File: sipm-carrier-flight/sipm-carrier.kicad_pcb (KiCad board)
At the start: 2 copper layers, 95 x 50 mm, 70 parts, among them J1 Conn_Coaxial_Small, J2 output, J3 Conn_02x02_Top_Bottom, U1 LTC6268xS8-10, U13 ADP7185ACPZN2.5-R7, U14 TPS7A2025PDBVR, U2 BUF602xD

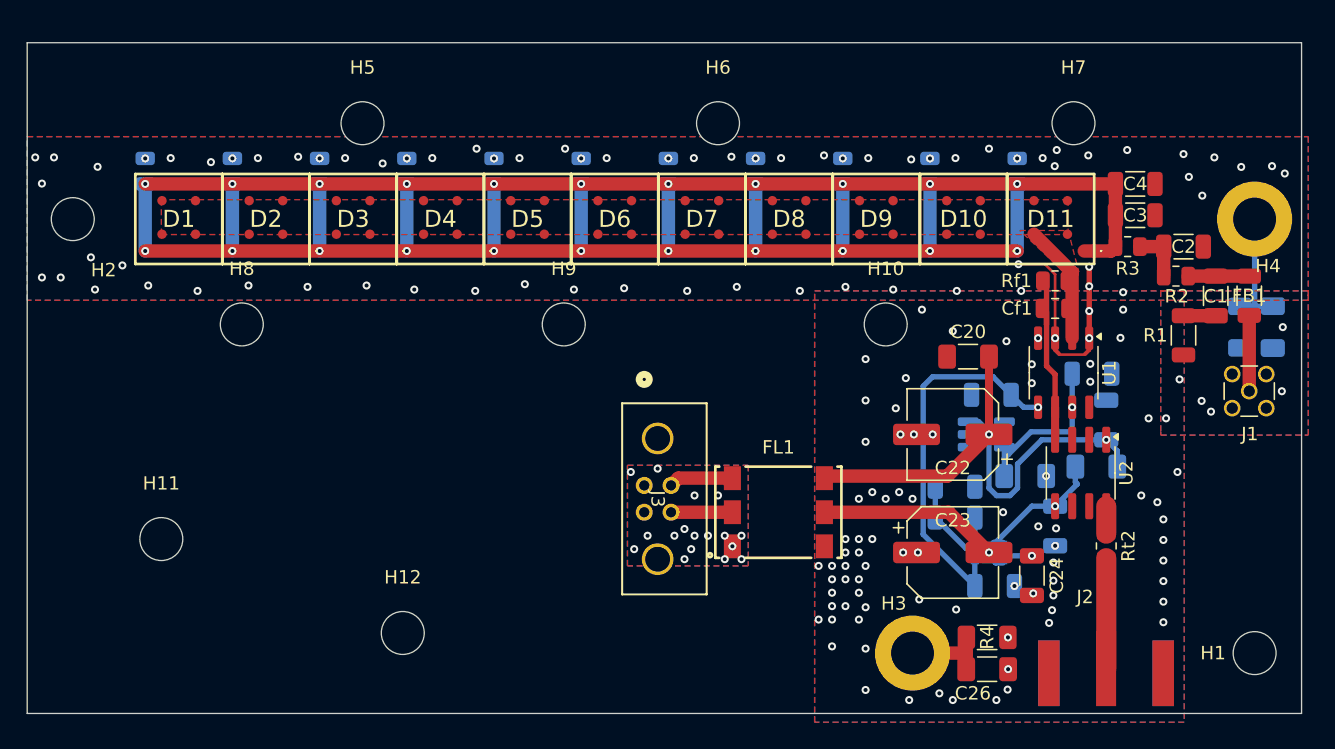
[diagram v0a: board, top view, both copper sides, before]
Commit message: updated per MSU comments
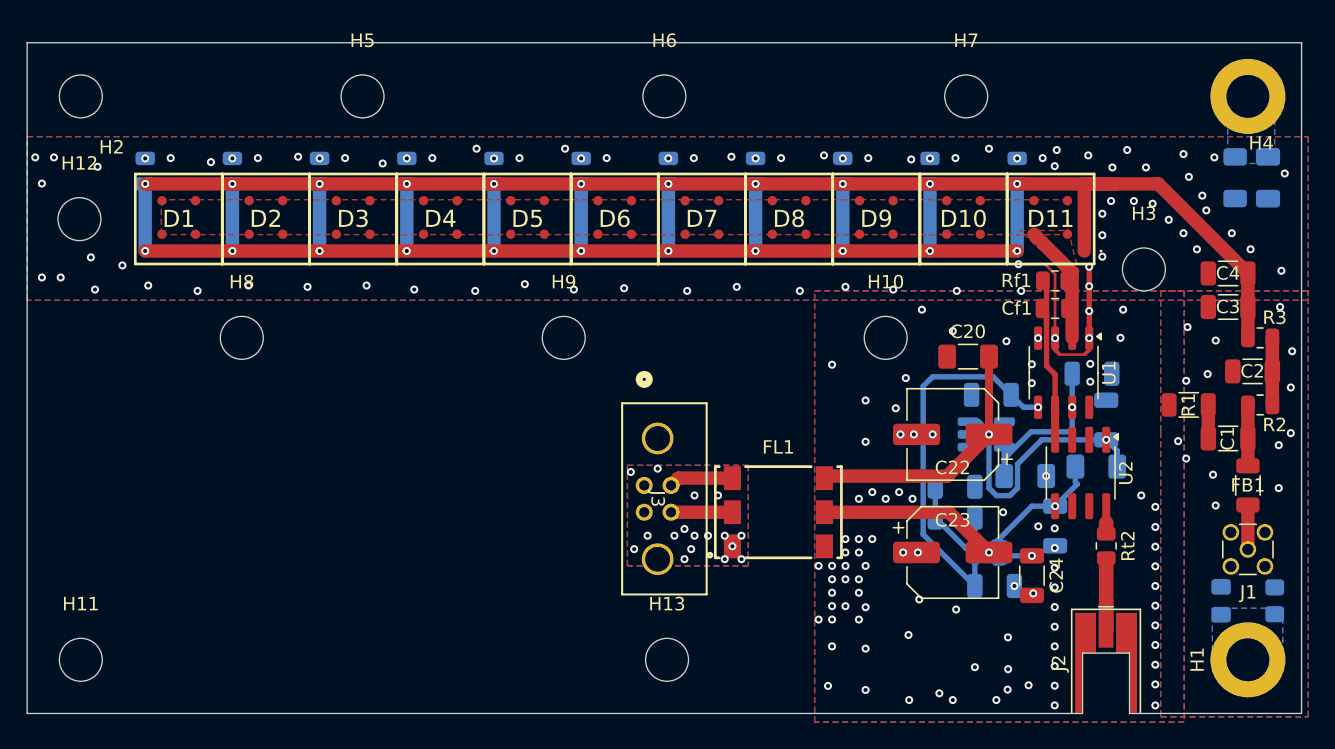
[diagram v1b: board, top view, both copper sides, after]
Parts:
- added H13: MountingHole, MountingHole:MountingHole_3.2mm_M3, F.Cu at (76.7, 72.0)
- C26: footprint Capacitor_SMD:C_1206_3216Metric_Pad1.33x1.80mm_HandSolder -> Capacitor_SMD:C_0805_2012Metric_Pad1.18x1.45mm_HandSolder; moved to B.Cu
- H1: value MountingHole -> MountingHole_Pad; footprint MountingHole:MountingHole_3.2mm_M3 -> MountingHole:MountingHole_3.2mm_M3_DIN965_Pad
- H3: value MountingHole_Pad -> MountingHole; footprint MountingHole:MountingHole_3.2mm_M3_DIN965_Pad -> MountingHole:MountingHole_3.2mm_M3
- J2: footprint Library:TE_CONSMA020.062-G -> Connector_Coaxial:MMCX_Molex_73415-0961_Horizontal_1.6mm-PCB
- R4: value 1.5Meg -> R_US; footprint Resistor_SMD:R_1206_3216Metric_Pad1.30x1.75mm_HandSolder -> Resistor_SMD:R_0805_2012Metric_Pad1.20x1.40mm_HandSolder; moved to B.Cu
- moved H12 39.1 mm to (32.9, 39.1)
- moved H3 33.4 mm to (112.2, 42.9)
- moved R4 21.6 mm to (122.0, 67.6), turned to -90 degrees
- moved C26 18.2 mm to (118.0, 67.6), turned to 90 degrees
- moved FB1 14.1 mm to (120.0, 59.0)
- moved R3 12.0 mm to (120.9, 48.0)
- moved J1 11.8 mm to (120.0, 63.8)
- moved R2 11.5 mm to (120.9, 53.0), turned to 180 degrees
- moved C27 11.1 mm to (121.5, 36.1)
- moved R5 11.1 mm to (119.0, 36.1)
- moved H11 10.8 mm to (33.0, 72.0)
- moved C1 10.7 mm to (118.5, 55.5), turned to 180 degrees
- moved C2 10.6 mm to (120.3, 50.5), turned to 180 degrees
- moved C3 9.73 mm to (118.5, 45.7), turned to 180 degrees
- moved C4 9.62 mm to (118.5, 43.2), turned to 180 degrees
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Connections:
- C26 pad 1: GND -> Net-(C26-Pad1)
- C26 pad 2: Net-(C26-Pad2) -> GND
- R4 pad 2: Net-(C26-Pad2) -> Net-(C26-Pad1)
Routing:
- net /Bias filter/bias_filtered: track 199.5 -> 217.1 mm
- net Net-(C27-Pad2): track 9.01 -> 0.00 mm
- net Net-(C26-Pad2): track 6.17 -> 0.00 mm
- net /driven TIA/amp_out: track 8.23 -> 5.30 mm
- net /Bias filter/bias_raw: track 5.64 -> 3.31 mm
- net Net-(Rt2-Pad1): track 2.05 -> 0.40 mm
- net Net-(C2-Pad1): track 3.97 -> 5.00 mm
- net -5V: track 26.9 -> 25.9 mm
- net Net-(FL1-1): track 5.56 -> 4.79 mm
- net GND: vias 160 -> 189
- added copper zone on B.Cu, net Net-(C26-Pad1)
- added copper zone on B.Cu, net Net-(C27-Pad2)
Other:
- outline, holes or cut-outs redrawn

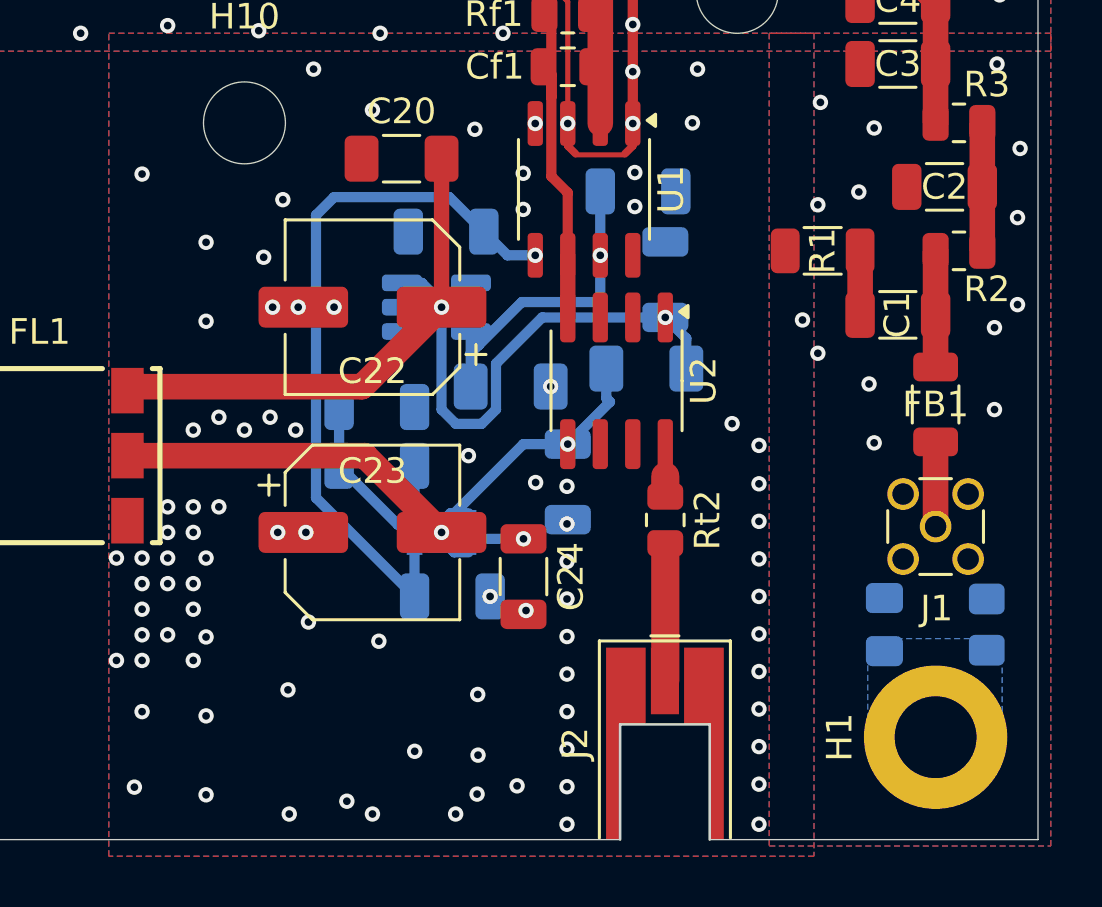
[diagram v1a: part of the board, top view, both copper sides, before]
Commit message: carrier OCD
- coplanar waveguide with ground at almost exactly 50 ohm output from the buffer, leading into termination resistor
- better ground return paths for the bias voltage
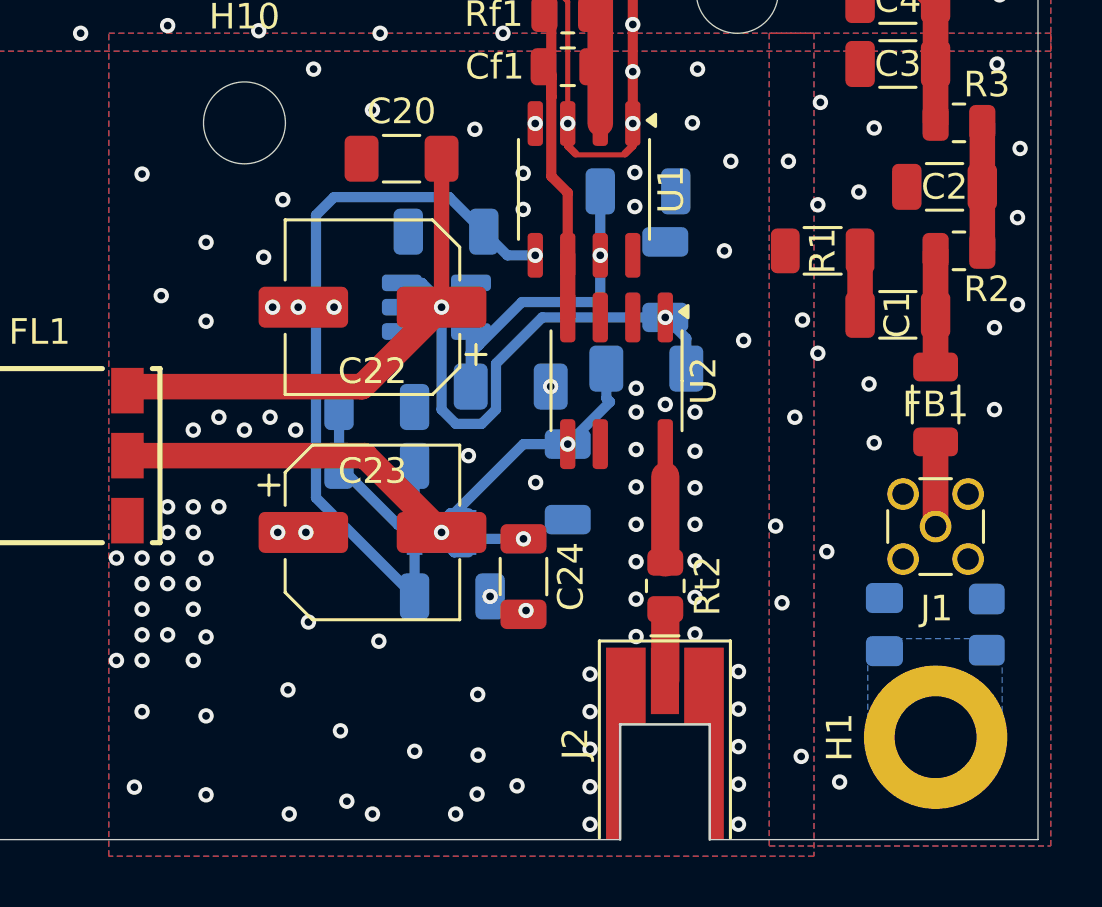
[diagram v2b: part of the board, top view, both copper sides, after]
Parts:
- moved Rt2 2.58 mm to (109.4, 66.1)
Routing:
- net Net-(Rt2-Pad1): track 0.40 -> 3.38 mm
- net /driven TIA/amp_out: track 5.30 -> 2.58 mm
- net GND: vias 189 -> 205

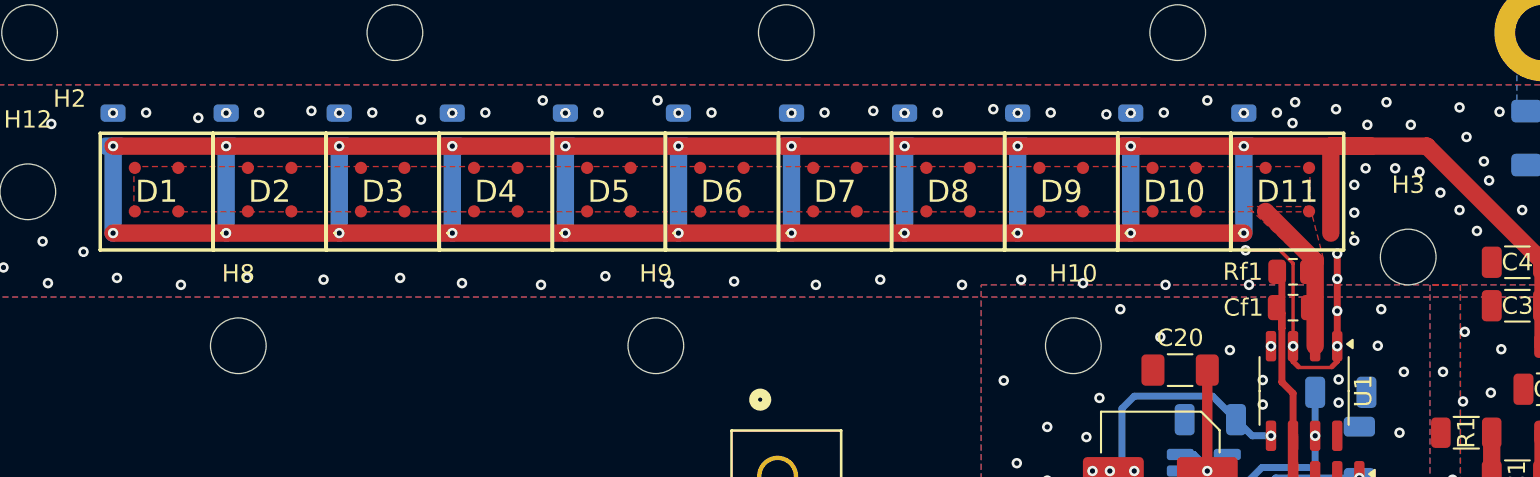
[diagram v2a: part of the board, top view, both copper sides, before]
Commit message: sipms: 0.04mm gap
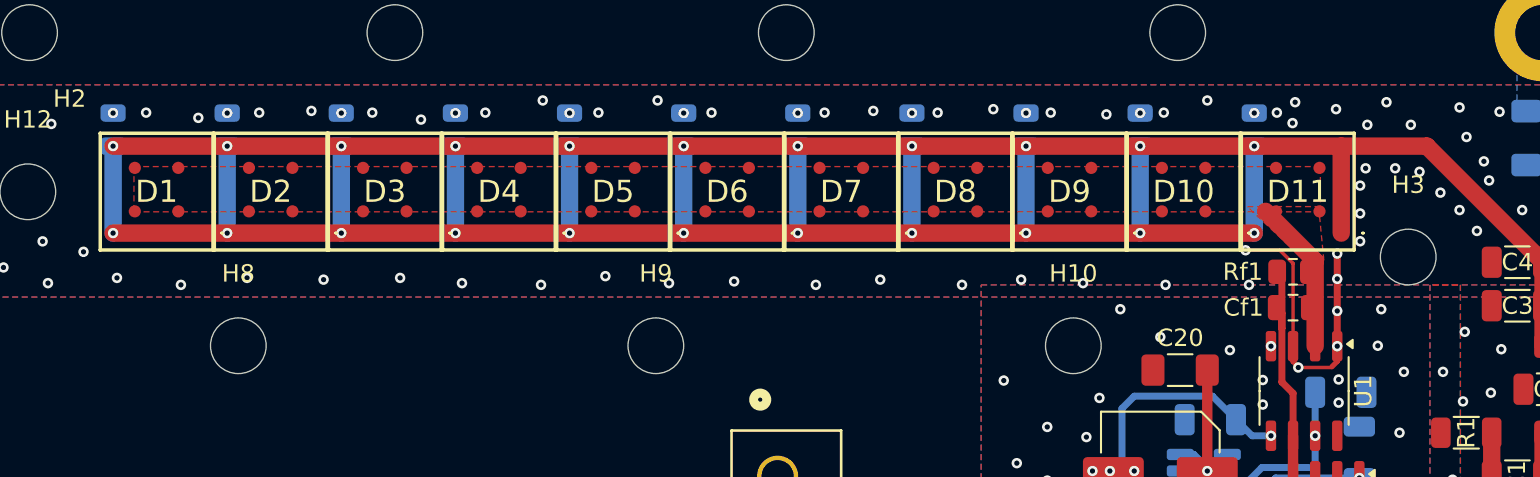
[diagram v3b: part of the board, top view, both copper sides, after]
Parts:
- moved C30 0.60 mm to (103.4, 35.6)
- moved D11 0.60 mm to (105.9, 39.0)
- moved C19 0.54 mm to (96.8, 35.6)
- moved D10 0.54 mm to (99.3, 39.0)
- moved C18 0.48 mm to (90.3, 35.6)
- moved D9 0.48 mm to (92.8, 39.0)
- moved C17 0.42 mm to (83.7, 35.6)
- moved D8 0.42 mm to (86.2, 39.0)
- moved C16 0.36 mm to (77.2, 35.6)
- moved D7 0.36 mm to (79.7, 39.0)
- moved C15 0.30 mm to (70.6, 35.6)
- moved D6 0.30 mm to (73.1, 39.0)
- moved C14 0.24 mm to (64.0, 35.6)
- moved D5 0.24 mm to (66.5, 39.0)
- moved C13 0.18 mm to (57.5, 35.6)
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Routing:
- net /Bias filter/bias_filtered: track 217.1 -> 215.4 mm

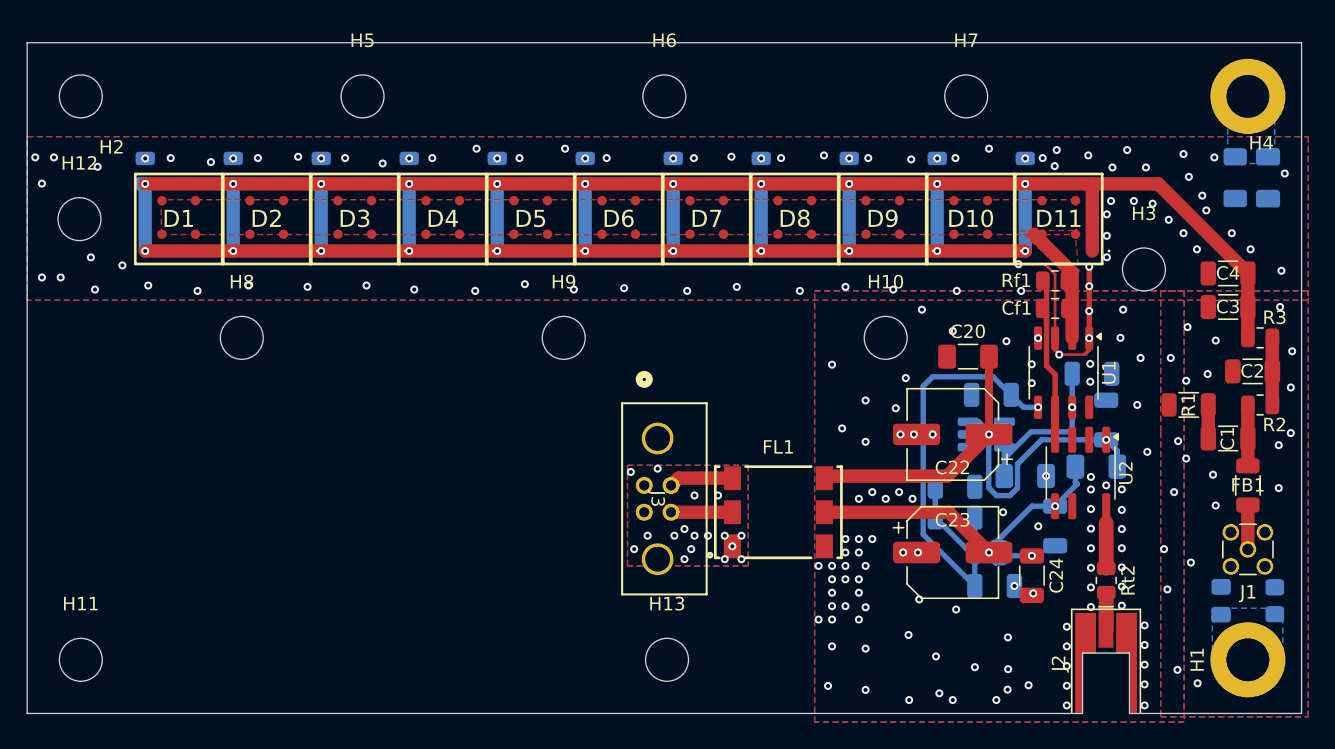
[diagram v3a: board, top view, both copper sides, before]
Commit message: sipm board pre-production
- verify spcaing between SiPMs
- move silkscreens around so that they are not overlapping
- change footprints to be hand-solder type in case someone has to do that
- change values of some components to unify part list (e.g. any 100n are now 0.1u)
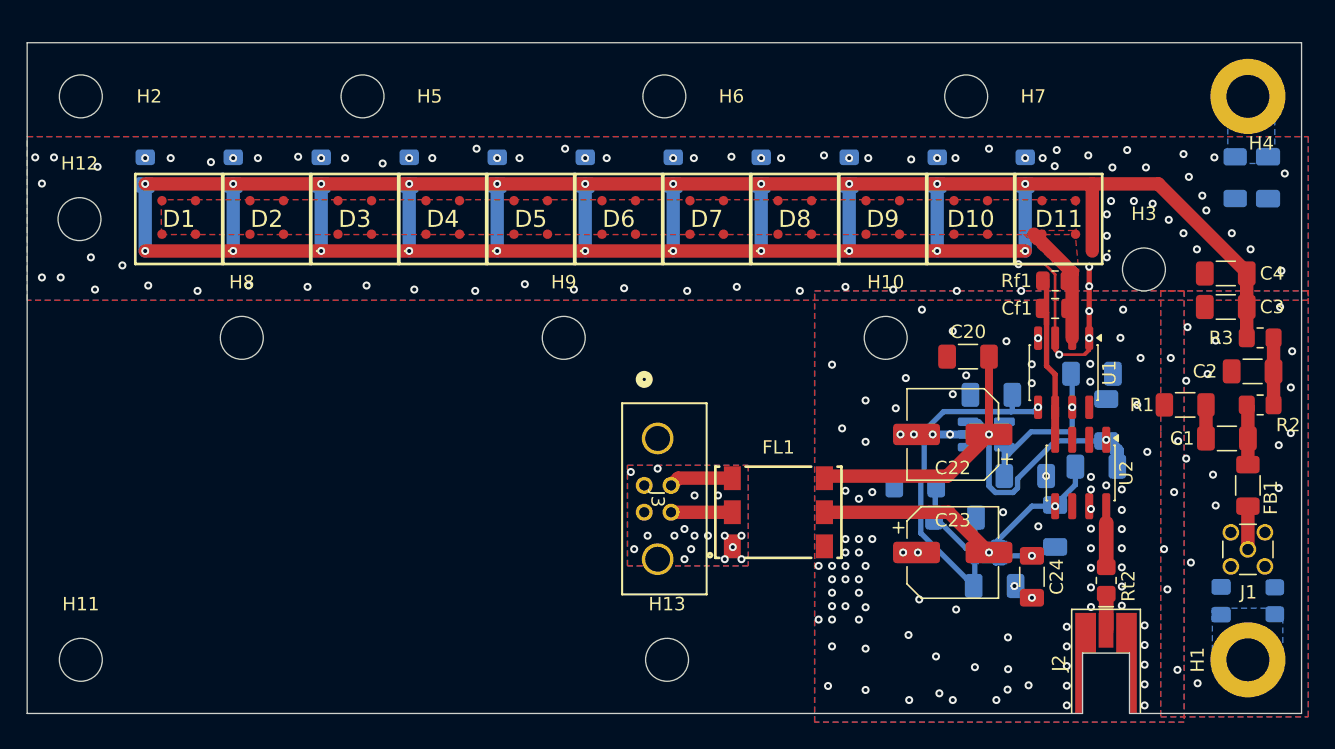
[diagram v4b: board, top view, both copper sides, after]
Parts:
- C1, C2, C24, C25, C28, C29, C4, C5, C6, C7, C8: footprint Capacitor_SMD:C_1206_3216Metric -> Capacitor_SMD:C_1206_3216Metric_Pad1.33x1.80mm_HandSolder
- C10, C11, C12, C13, C14, C15, C16, C17, C18, C19, C30: footprint Capacitor_SMD:C_0805_2012Metric -> Capacitor_SMD:C_0805_2012Metric_Pad1.18x1.45mm_HandSolder
- C3: value 100n -> 0.1u; footprint Capacitor_SMD:C_1206_3216Metric -> Capacitor_SMD:C_1206_3216Metric_Pad1.33x1.80mm_HandSolder
- FB1, R1: footprint Resistor_SMD:R_1206_3216Metric -> Resistor_SMD:R_1206_3216Metric_Pad1.30x1.75mm_HandSolder
- R2, R3, Rt2: footprint Resistor_SMD:R_0805_2012Metric -> Resistor_SMD:R_0805_2012Metric_Pad1.20x1.40mm_HandSolder
- moved C29 2.97 mm to (95.2, 59.0), turned to 180 degrees
- moved R1 0.26 mm to (115.3, 53.0)
- moved C3 0.18 mm to (118.3, 45.7)
- moved C4 0.18 mm to (118.3, 43.2)
- moved C1 0.09 mm to (118.4, 55.5)
- moved C24 0.09 mm to (103.9, 65.8)
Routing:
- net GND: track 17.7 -> 20.3 mm, vias 205 -> 206
- net +5V: track 45.3 -> 44.4 mm
- net -2V5: track 28.5 -> 27.8 mm
